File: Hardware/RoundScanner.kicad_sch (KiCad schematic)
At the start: 0 parts

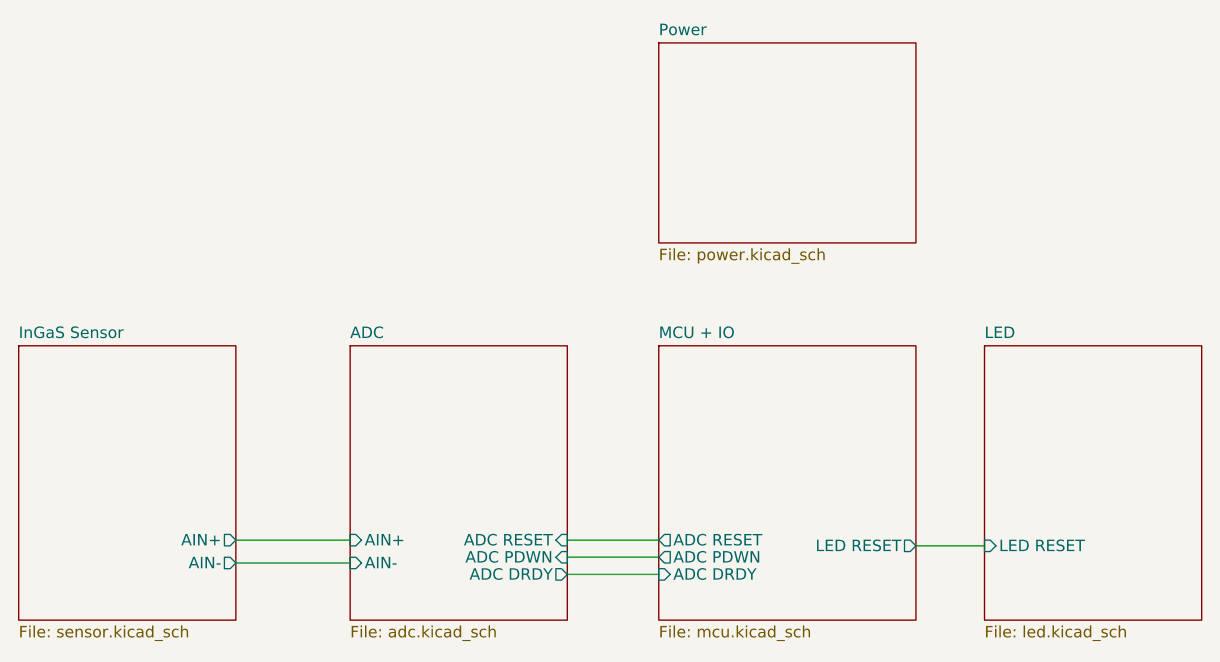
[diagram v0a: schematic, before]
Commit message: Version 0.6 - 4 layer version
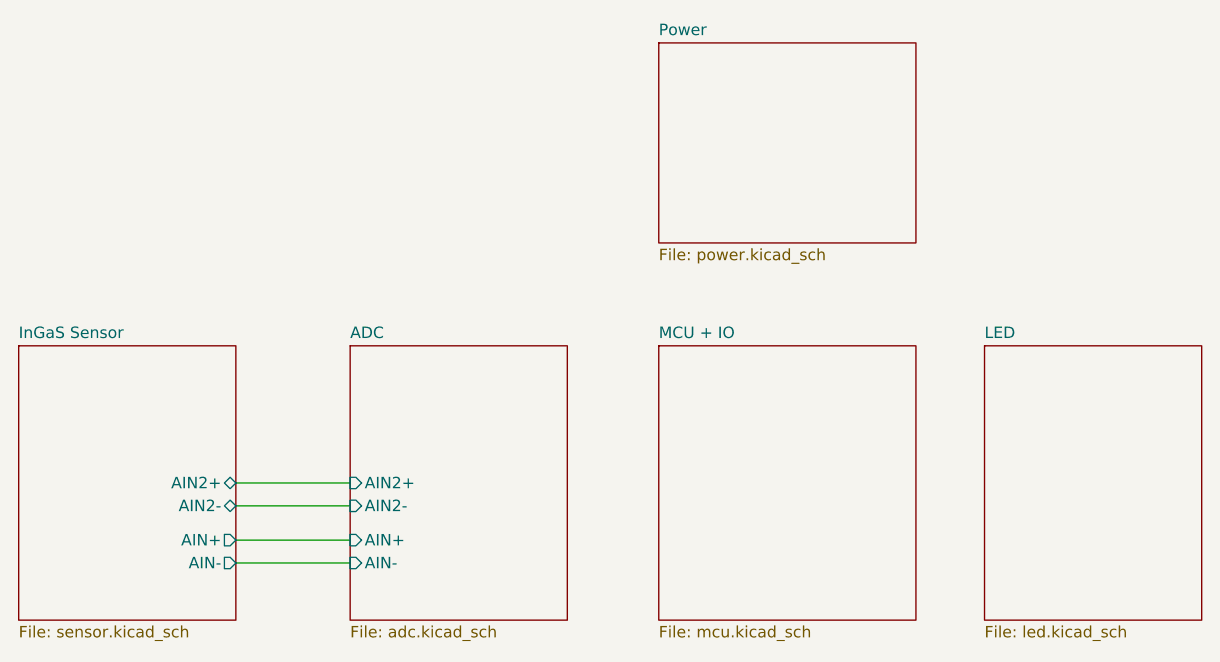
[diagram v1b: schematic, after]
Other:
- sheet ADC ports: added AIN2+, AIN2-; removed ADC DRDY, ADC PDWN, ADC RESET
- sheet InGaS Sensor ports: added AIN2+, AIN2-; removed none
- sheet LED ports: added none; removed LED RESET
- sheet MCU + IO ports: added none; removed ADC DRDY, ADC PDWN, ADC RESET, LED RESET
